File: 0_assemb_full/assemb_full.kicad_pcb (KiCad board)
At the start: 2 copper layers, 100.3 x 100.3 mm, 155 parts, among them J1 BarrelJack, J10 SPIConn_01x03, J11 OutToRPi, J12 LEDConn_01x05, J13 RPiConn_01x03, J2 Conn_02x06, J3 AudioJack3, J4 Servo0Conn_01x03, J5 Servo1Conn_01x03, J6 Servo2Conn_01x03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

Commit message: Made adjustments according to presentation feedback. Almost ready for teaching team to look over.
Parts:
- removed J13: RPiConn_01x03, Connector_PinSocket_2.54mm:PinSocket_1x03_P2.54mm_Vertical
- added TP12: GPIO1, TestPoint:TestPoint_THTPad_2.0x2.0mm_Drill1.0mm, F.Cu at (129.2, 104.1)
- added TP13: GPIO4, TestPoint:TestPoint_THTPad_2.0x2.0mm_Drill1.0mm, F.Cu at (127.6, 93.2)
- added TP14: GPIO2, TestPoint:TestPoint_THTPad_2.0x2.0mm_Drill1.0mm, F.Cu at (133.3, 102.0)
- added TP15: GPIO5, TestPoint:TestPoint_THTPad_2.0x2.0mm_Drill1.0mm, F.Cu at (124.1, 93.2)
- added TP16: GPIO3, TestPoint:TestPoint_THTPad_2.0x2.0mm_Drill1.0mm, F.Cu at (129.2, 99.9)
- added TP17: GPIO6, TestPoint:TestPoint_THTPad_2.0x2.0mm_Drill1.0mm, F.Cu at (120.4, 93.2)
- TP10, TP11, TP8, TP9: footprint TestPoint:TestPoint_THTPad_1.5x1.5mm_Drill0.7mm -> TestPoint:TestPoint_THTPad_2.0x2.0mm_Drill1.0mm
- TP7: value TestPoint -> MOSI; footprint TestPoint:TestPoint_THTPad_1.5x1.5mm_Drill0.7mm -> TestPoint:TestPoint_THTPad_2.0x2.0mm_Drill1.0mm
- moved R13 4.62 mm to (132.7, 108.8)
- moved D2 4.62 mm to (133.7, 105.5)
- moved C1 2.90 mm to (86.1, 95.8), turned to 0 degrees
- moved C17 1.17 mm to (125.2, 100.8)
- moved TP10 0.84 mm to (132.7, 177.5)
- moved C36 0.37 mm to (60.5, 154.4)
- moved REF** 0.32 mm to (87.4, 130.5)
- moved REF** 0.32 mm to (84.4, 130.5)
- moved C4 0.25 mm to (102.6, 160.3)
- moved C5 0.25 mm to (110.8, 160.3)
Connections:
- U5 pad 56: unconnected-(U5-Pad56) -> /STM32 Interface/GPIO1
- U5 pad 57: unconnected-(U5-Pad57) -> /STM32 Interface/GPIO2
- U5 pad 58: unconnected-(U5-Pad58) -> /STM32 Interface/GPIO3
- U5 pad 59: /STM32 Interface/GPIO1 -> /STM32 Interface/GPIO4
- U5 pad 61: /STM32 Interface/GPIO2 -> /STM32 Interface/GPIO5
- U5 pad 62: /STM32 Interface/GPIO3 -> /STM32 Interface/GPIO6
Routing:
- net /STM32 Interface/GPIO4: track 0.00 -> 23.6 mm, vias 0 -> 2
- net /STM32 Interface/GPIO5: track 0.00 -> 21.7 mm, vias 0 -> 2
- net GND: track 97.0 -> 111.8 mm, vias 30 -> 38
- net /STM32 Interface/GPIO6: track 0.00 -> 12.3 mm
- net /STM32 Interface/GPIO3: track 13.9 -> 21.6 mm, vias 0 -> 1
- net /STM32 Interface/GPIO2: track 18.1 -> 24.2 mm, vias 2 -> 0
- net ADC_HP: track 158.1 -> 154.5 mm
- net 3_3V: track 146.5 -> 149.5 mm
- net Net-(C36-Pad2): track 4.86 -> 5.76 mm
- net /STM32 Interface/GPIO1: track 25.2 -> 26.0 mm, vias 0 -> 1
- net Net-(C9-Pad1): track 12.2 -> 11.4 mm
- net /High and Low Pass/LP Pre-LP: track 33.7 -> 32.9 mm
- net Audio_In_Tip: track 60.9 -> 60.3 mm
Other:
- board text added: "5"
- board text added: "6"
- board text added: "ECE477 Team 10 Julian Kang, Lydia Allen, Ryan Davitt, Vivek Panchagnula Main Board (REV1.1, 3-5-2024)"
- board text removed: "ECE477 Team 10 Julian Kang, Lydia Allen, Ryan Davitt, Vivek Panchagnula Main Board (REV1.0, 2-27-2024)"

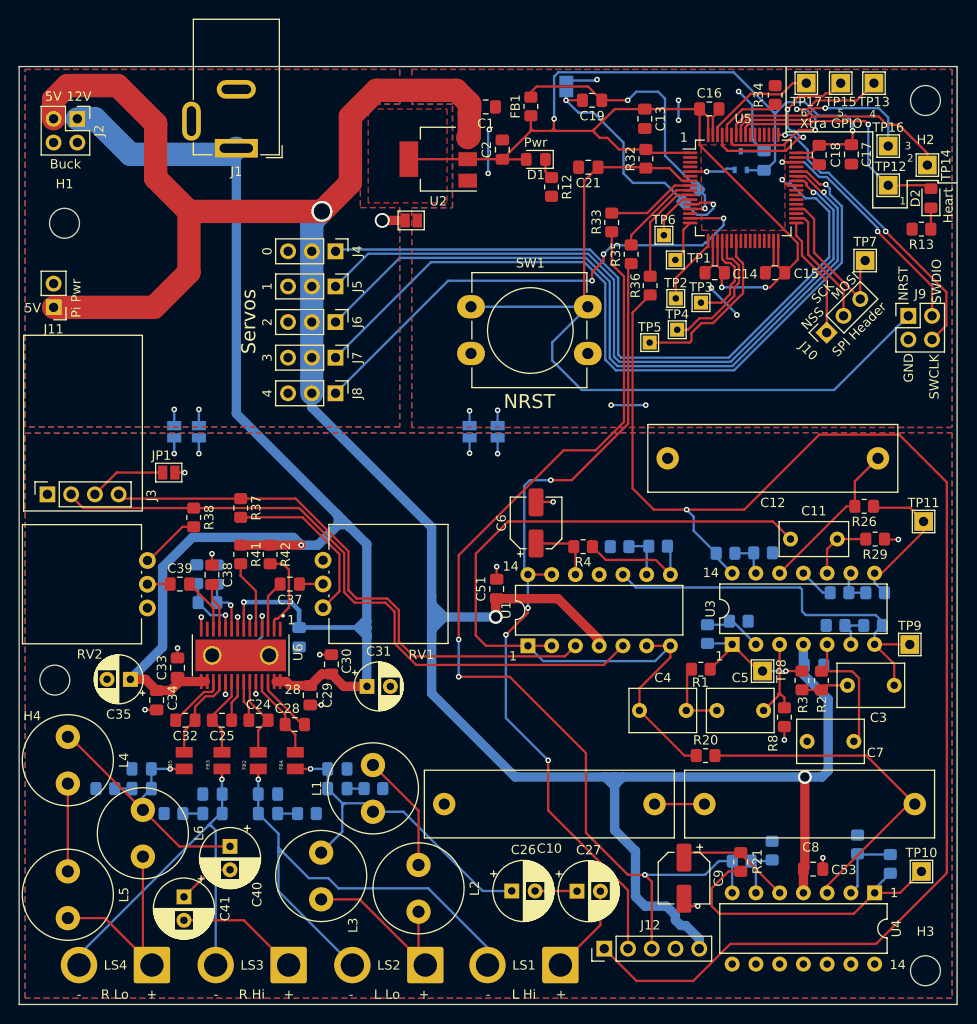
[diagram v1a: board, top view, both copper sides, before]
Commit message: Fixed LED Board and added GND to SPI on Main Board
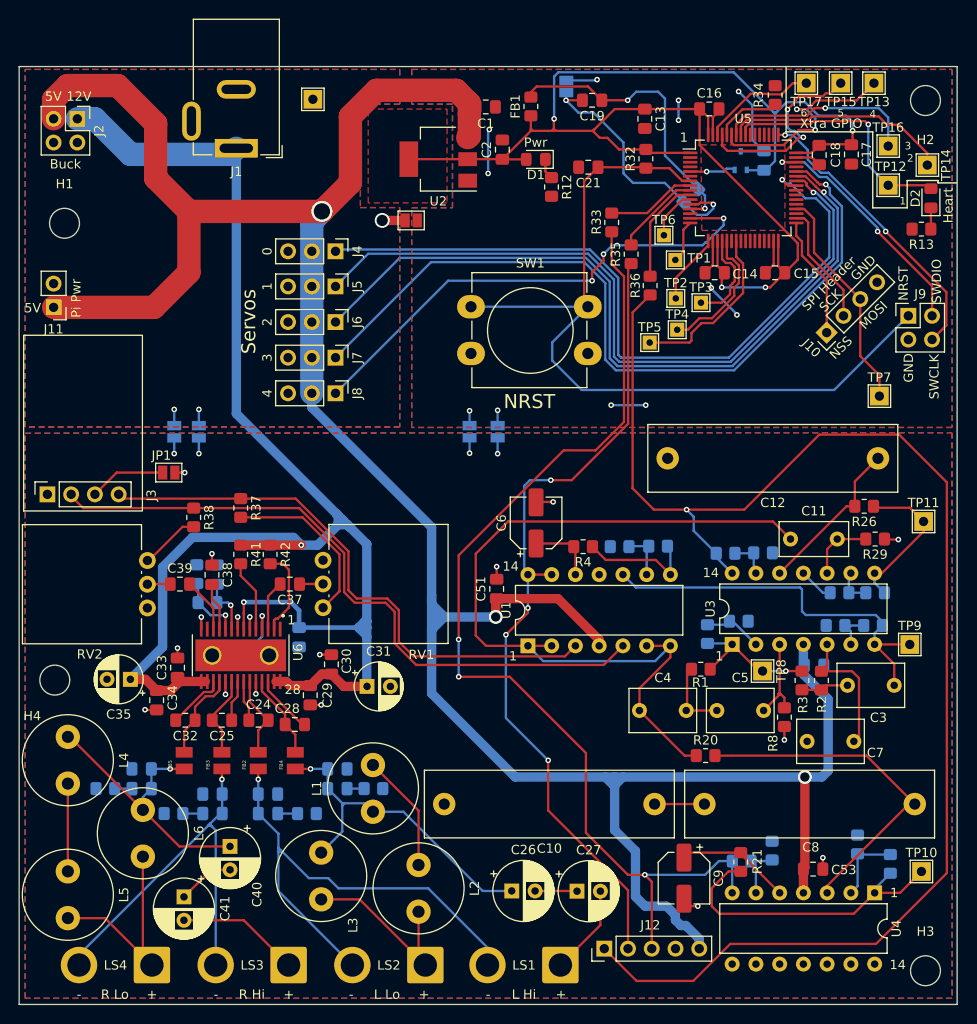
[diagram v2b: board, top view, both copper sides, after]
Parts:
- added REF**: TestPoint_THTPad_2.0x2.0mm_Drill1.0mm, TestPoint:TestPoint_THTPad_2.0x2.0mm_Drill1.0mm, F.Cu at (67.6, 94.9)
- J10: footprint Connector_PinSocket_2.54mm:PinSocket_1x03_P2.54mm_Vertical -> Connector_PinHeader_2.54mm:PinHeader_1x04_P2.54mm_Vertical
- moved TP7 14.6 mm to (128.2, 126.7)
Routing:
- net /STM32 Interface/SPI_MOSI: track 16.6 -> 24.2 mm
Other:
- board text added: "ECE477 Team 10 Julian Kang, Lydia Allen, Ryan Davitt, Vivek Panchagnula Main Board (REV1.2, 3-7-2024)"
- board text removed: "ECE477 Team 10 Julian Kang, Lydia Allen, Ryan Davitt, Vivek Panchagnula Main Board (REV1.1, 3-5-2024)"
